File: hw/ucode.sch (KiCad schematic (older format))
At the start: 14 parts, among them U501 74HC393, U502 74HCT02, U504 74HCT238, U505 74HCT238, U506 27C64, U507 27C64, U508 27C64, U509 74HCT175, U510 74HCT175, U511 74HCT175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

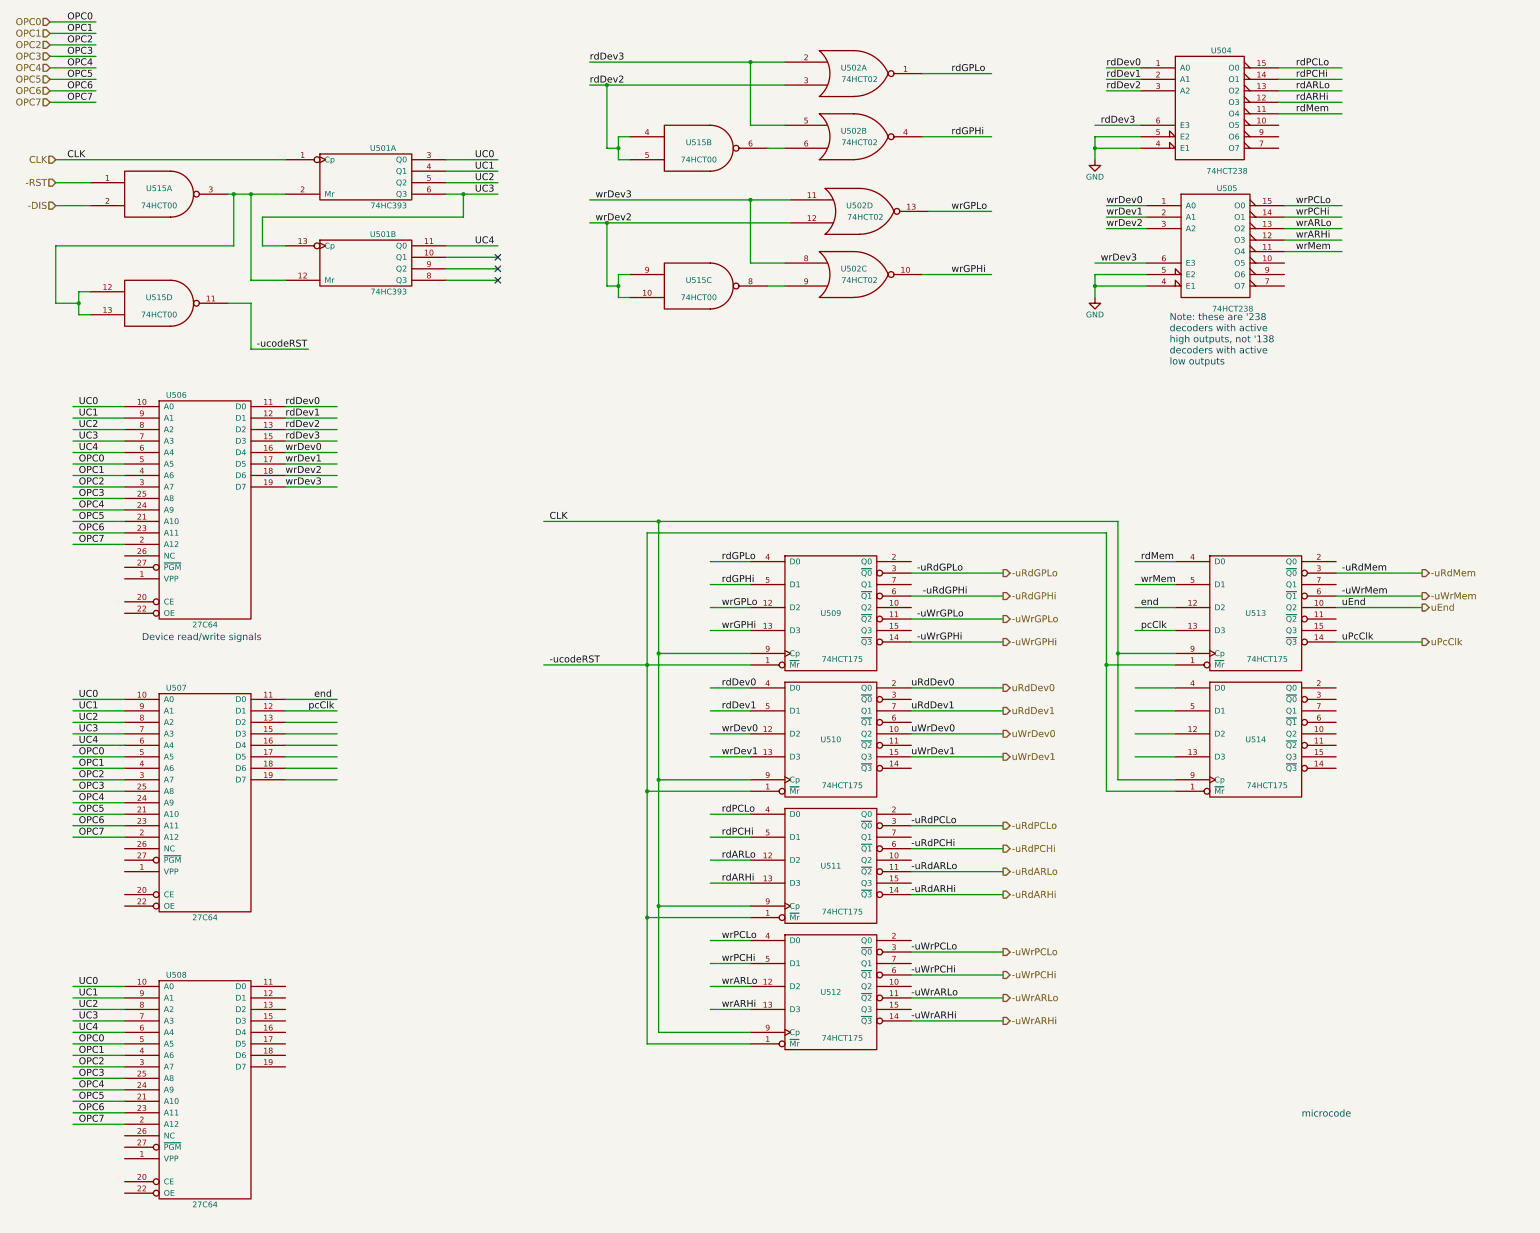
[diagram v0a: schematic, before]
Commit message: use 74HC590 as microcode program counter
The 74HC393 can only advance bit 5 using a ripple
carry from the lower 4 bit counter, which I am
concerned would be too slow (especially given the
slowness of the microcode EPROMS, which
must generate a value output within a half
of one clock cycle).  The 74HC590 is a
proper 8 bit counter, which I assume has fast
carry logic internally.
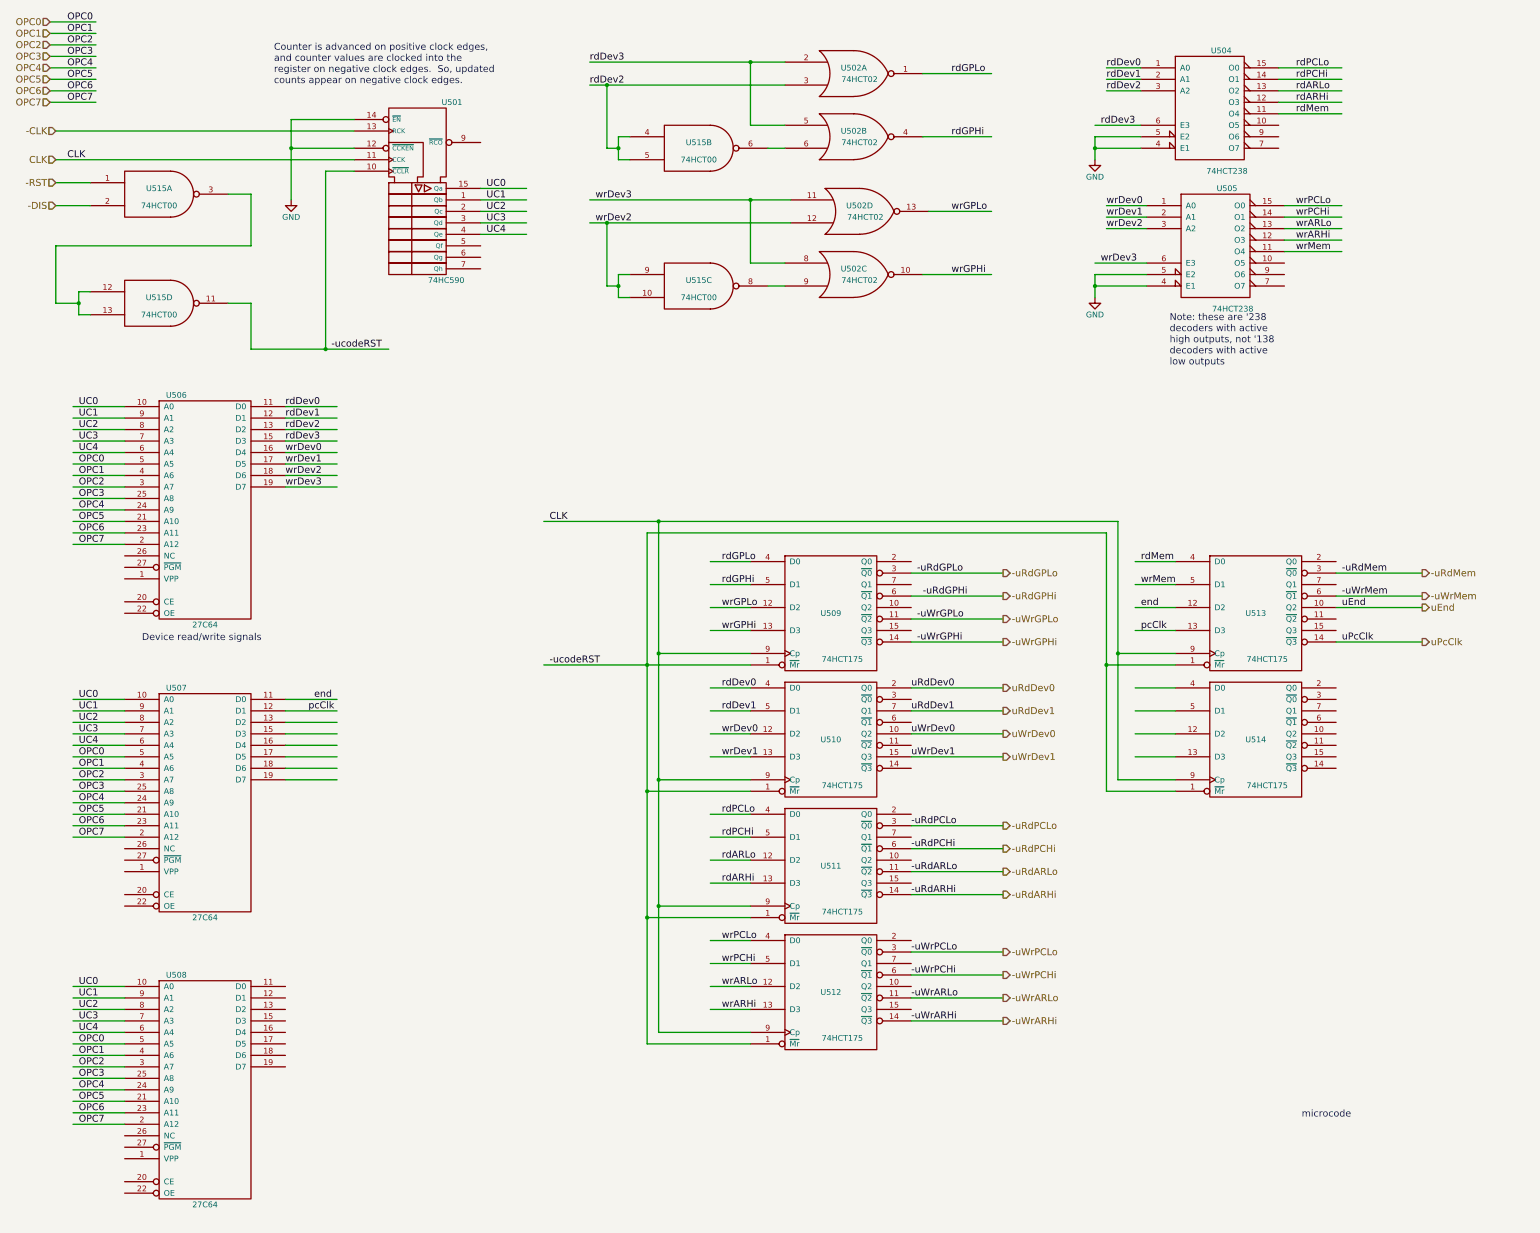
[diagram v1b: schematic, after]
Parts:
- removed U501: 74HC393, symbol 74LS393
- added U501: 74HC590, symbol 74LS590
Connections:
- net labels added: -CLK
- wire segments 223 -> 198
- no-connect marks 3 -> 0
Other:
- note added: "Counter is advanced on positive clock edges,\nand counter values are clocked into the\nregister on negative clock edges. So, updated\ncounts appear on negative clock edges."
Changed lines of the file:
@@
 LIBS:valves
 LIBS:switches
+LIBS:ttl_ieee
 LIBS:cpu2-cache
 EELAYER 25 0
@@
 	1    0    0    -1
 $EndComp
-$Comp
-L 74LS393 U501
-U 1 1 592C73B2
-P 3800 2000
-F 0 "U501" H 3950 2250 50  0000 C CNN
-F 1 "74HC393" H 4000 1750 50  0000 C CNN
-F 2 "" H 3800 2000 50  0000 C CNN
-F 3 "" H 3800 2000 50  0000 C CNN
-	1    3800 2000
-	1    0    0    -1
-$EndComp
-$Comp
-L 74LS393 U501
-U 2 1 592C73E9
-P 3800 2750
-F 0 "U501" H 3950 3000 50  0000 C CNN
-F 1 "74HC393" H 4000 2500 50  0000 C CNN
-F 2 "" H 3800 2750 50  0000 C CNN
-F 3 "" H 3800 2750 50  0000 C CNN
-	2    3800 2750
-	1    0    0    -1
-$EndComp
 Text Label 1200 650  0    60   ~ 0
 OPC0
@@
 Text Label 1200 1350 0    60   ~ 0
 OPC7
-Text Label 4750 1850 0    60   ~ 0
-UC0
-Text Label 4750 1950 0    60   ~ 0
-UC1
-Text Label 4750 2050 0    60   ~ 0
-UC2
-Text Label 4750 2150 0    60   ~ 0
-UC3
-Text Label 4750 2600 0    60   ~ 0
-UC4
 Text Label 1300 4000 0    60   ~ 0
 UC0
@@
 Text Label 1300 10250 0    60   ~ 0
 OPC7
-NoConn ~ 4950 2700
-NoConn ~ 4950 2800
-NoConn ~ 4950 2900
 Text Notes 11950 10200 0    60   ~ 0
 microcode
@@
 	1050 1350 1450 1350
 Wire Wire Line
-	4500 2150 4650 2150
-Wire Wire Line
-	4650 2150 4950 2150
-Wire Wire Line
-	4650 2150 4650 2350
-Wire Wire Line
-	4650 2350 2900 2350
-Wire Wire Line
-	2900 2350 2900 2600
-Wire Wire Line
-	2900 2600 3100 2600
-Wire Wire Line
-	4500 1850 4950 1850
-Wire Wire Line
-	4500 1950 4950 1950
-Wire Wire Line
-	4500 2050 4950 2050
-Connection ~ 4650 2150
-Wire Wire Line
-	4500 2600 4950 2600
-Wire Wire Line
 	1700 4000 1250 4000
 Wire Wire Line
@@
 	1700 10250 1250 10250
 Wire Wire Line
-	4500 2700 4950 2700
-Wire Wire Line
-	4500 2800 4950 2800
-Wire Wire Line
-	4500 2900 4950 2900
-Wire Wire Line
-	2600 2150 2650 2150
-Wire Wire Line
-	2650 2150 2800 2150
-Wire Wire Line
-	2800 2150 3100 2150
-Wire Wire Line
-	3100 2900 2800 2900
-Wire Wire Line
-	2800 2900 2800 2150
-Connection ~ 2800 2150
-Wire Wire Line
-	1100 1850 3100 1850
+	1100 1850 3700 1850
 Wire Wire Line
 	3100 4000 3550 4000
@@
 	10150 1750 10550 1750
 Wire Wire Line
-	10150 1650 10150 1750
-Wire Wire Line
-	10150 1750 10150 1850
+	10150 1650 10150 1850
 Wire Wire Line
 	10550 1050 10250 1050
@@
 	10600 2950 10150 2950
 Wire Wire Line
-	10150 2850 10150 2950
-Wire Wire Line
-	10150 2950 10150 3050
+	10150 2850 10150 3050
 Wire Wire Line
 	11800 2250 12300 2250
@@
 	11800 2650 12300 2650
 Wire Wire Line
-	5750 1000 7150 1000
-Wire Wire Line
-	7150 1000 7450 1000
-Wire Wire Line
-	5750 1200 5900 1200
-Wire Wire Line
-	5900 1200 7450 1200
-Wire Wire Line
-	5750 2200 7150 2200
-Wire Wire Line
-	7150 2200 7500 2200
-Wire Wire Line
-	5750 2400 5900 2400
-Wire Wire Line
-	5900 2400 7500 2400
+	5750 1000 7450 1000
+Wire Wire Line
+	5750 1200 7450 1200
+Wire Wire Line
+	5750 2200 7500 2200
+Wire Wire Line
+	5750 2400 7500 2400
 Wire Wire Line
 	8650 1100 9250 1100
@@
 	6100 2850 6000 2850
 Wire Wire Line
-	6000 2850 6000 2950
-Wire Wire Line
-	6000 2950 6000 3050
+	6000 2850 6000 3050
 Wire Wire Line
 	6000 2950 5900 2950
@@
 	1400 3000 1300 3000
 Wire Wire Line
-	1300 3000 1300 3100
-Wire Wire Line
-	1300 3100 1300 3200
+	1300 3000 1300 3200
 Wire Wire Line
 	1300 3100 1100 3100
@@
 	1100 3100 1100 2600
 Wire Wire Line
-	1100 2600 2650 2600
-Wire Wire Line
-	2650 2600 2650 2150
-Connection ~ 2650 2150
+	1100 2600 2800 2600
+Wire Wire Line
+	2800 2600 2800 2150
 Wire Wire Line
 	1300 3200 1400 3200
@@
 	2800 3100 2800 3500
 Wire Wire Line
-	2800 3500 3300 3500
-Text Label 2850 3500 0    60   ~ 0
+	2800 3500 4000 3500
+Text Label 3500 3500 0    60   ~ 0
 -ucodeRST
 Wire Wire Line
-	5350 6250 6250 6250
-Wire Wire Line
-	6250 6250 7150 6250
+	5350 6250 7150 6250
 Text Label 5400 6250 0    60   ~ 0
 -ucodeRST
@@
 	6250 7350 7150 7350
 Wire Wire Line
-	6250 5100 6250 6250
-Wire Wire Line
-	6250 6250 6250 7350
-Wire Wire Line
-	6250 7350 6250 8450
-Wire Wire Line
-	6250 8450 6250 9550
+	6250 5100 6250 9550
 Connection ~ 6250 6250
 Wire Wire Line
@@
 	10850 6250 10250 6250
 Wire Wire Line
-	10250 5100 10250 6250
-Wire Wire Line
-	10250 6250 10250 7350
+	10250 5100 10250 7350
 Wire Wire Line
 	10250 5100 6250 5100
@@
 	7150 6150 6350 6150
 Wire Wire Line
-	6350 5000 6350 6150
-Wire Wire Line
-	6350 6150 6350 7250
-Wire Wire Line
-	6350 7250 6350 8350
-Wire Wire Line
-	6350 8350 6350 9450
-Wire Wire Line
-	5350 5000 6350 5000
-Wire Wire Line
-	6350 5000 10350 5000
+	6350 5000 6350 9450
+Wire Wire Line
+	5350 5000 10350 5000
 Text Label 5400 5000 0    60   ~ 0
 CLK
@@
 	10850 6150 10350 6150
 Wire Wire Line
-	10350 5000 10350 6150
-Wire Wire Line
-	10350 6150 10350 7250
+	10350 5000 10350 7250
 Connection ~ 6350 5000
 Wire Wire Line
@@
 	6000 1750 5900 1750
 Wire Wire Line
-	6000 1650 6000 1750
-Wire Wire Line
-	6000 1750 6000 1850
+	6000 1650 6000 1850
 Wire Wire Line
 	6100 1650 6000 1650
@@
 	1    0    0    -1
 $EndComp
+$Comp
+L 74LS590 U501
+U 1 1 594FEAE3
+P 4250 2150
+F 0 "U501" H 4550 2950 50  0000 C CNN
+F 1 "74HC590" H 4500 1400 50  0000 C CNN
+F 2 "" H 4250 2150 60  0000 C CNN
+F 3 "" H 4250 2150 60  0000 C CNN
+	1    4250 2150
+	1    0    0    -1
+$EndComp
+Text HLabel 1100 1600 0    60   Input ~ 0
+-CLK
+Wire Wire Line
+	3700 1600 1100 1600
+Wire Wire Line
+	3700 1950 3450 1950
+Wire Wire Line
+	3450 1950 3450 3500
+Connection ~ 3450 3500
+Wire Wire Line
+	2800 2150 2600 2150
+Wire Wire Line
+	3700 1750 3150 1750
+Wire Wire Line
+	3150 1500 3150 2200
+Wire Wire Line
+	3700 1500 3150 1500
+Connection ~ 3150 1750
+Wire Wire Line
+	4800 2100 5200 2100
+Wire Wire Line
+	4800 2200 5200 2200
+Wire Wire Line
+	4800 2300 5200 2300
+Wire Wire Line
+	4800 2400 5200 2400
+Wire Wire Line
+	4800 2500 5200 2500
+Text Label 4850 2100 0    60   ~ 0
+UC0
+Text Label 4850 2200 0    60   ~ 0
+UC1
+Text Label 4850 2300 0    60   ~ 0
+UC2
+Text Label 4850 2400 0    60   ~ 0
+UC3
+Text Label 4850 2500 0    60   ~ 0
+UC4
+$Comp
+L GND #PWR?
+U 1 1 59500711
+P 3150 2200
+F 0 "#PWR?" H 3150 1950 50  0001 C CNN
+F 1 "GND" H 3150 2050 50  0000 C CNN
+F 2 "" H 3150 2200 50  0001 C CNN
+F 3 "" H 3150 2200 50  0001 C CNN
+	1    3150 2200
+	1    0    0    -1
+$EndComp
+Text Notes 3000 1200 0    60   ~ 0
+Counter is advanced on positive clock edges,\nand counter values are clocked into the\nregister on negative clock edges.  So, updated\ncounts appear on negative clock edges.
 $EndSCHEMATC

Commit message: redoing device read logic
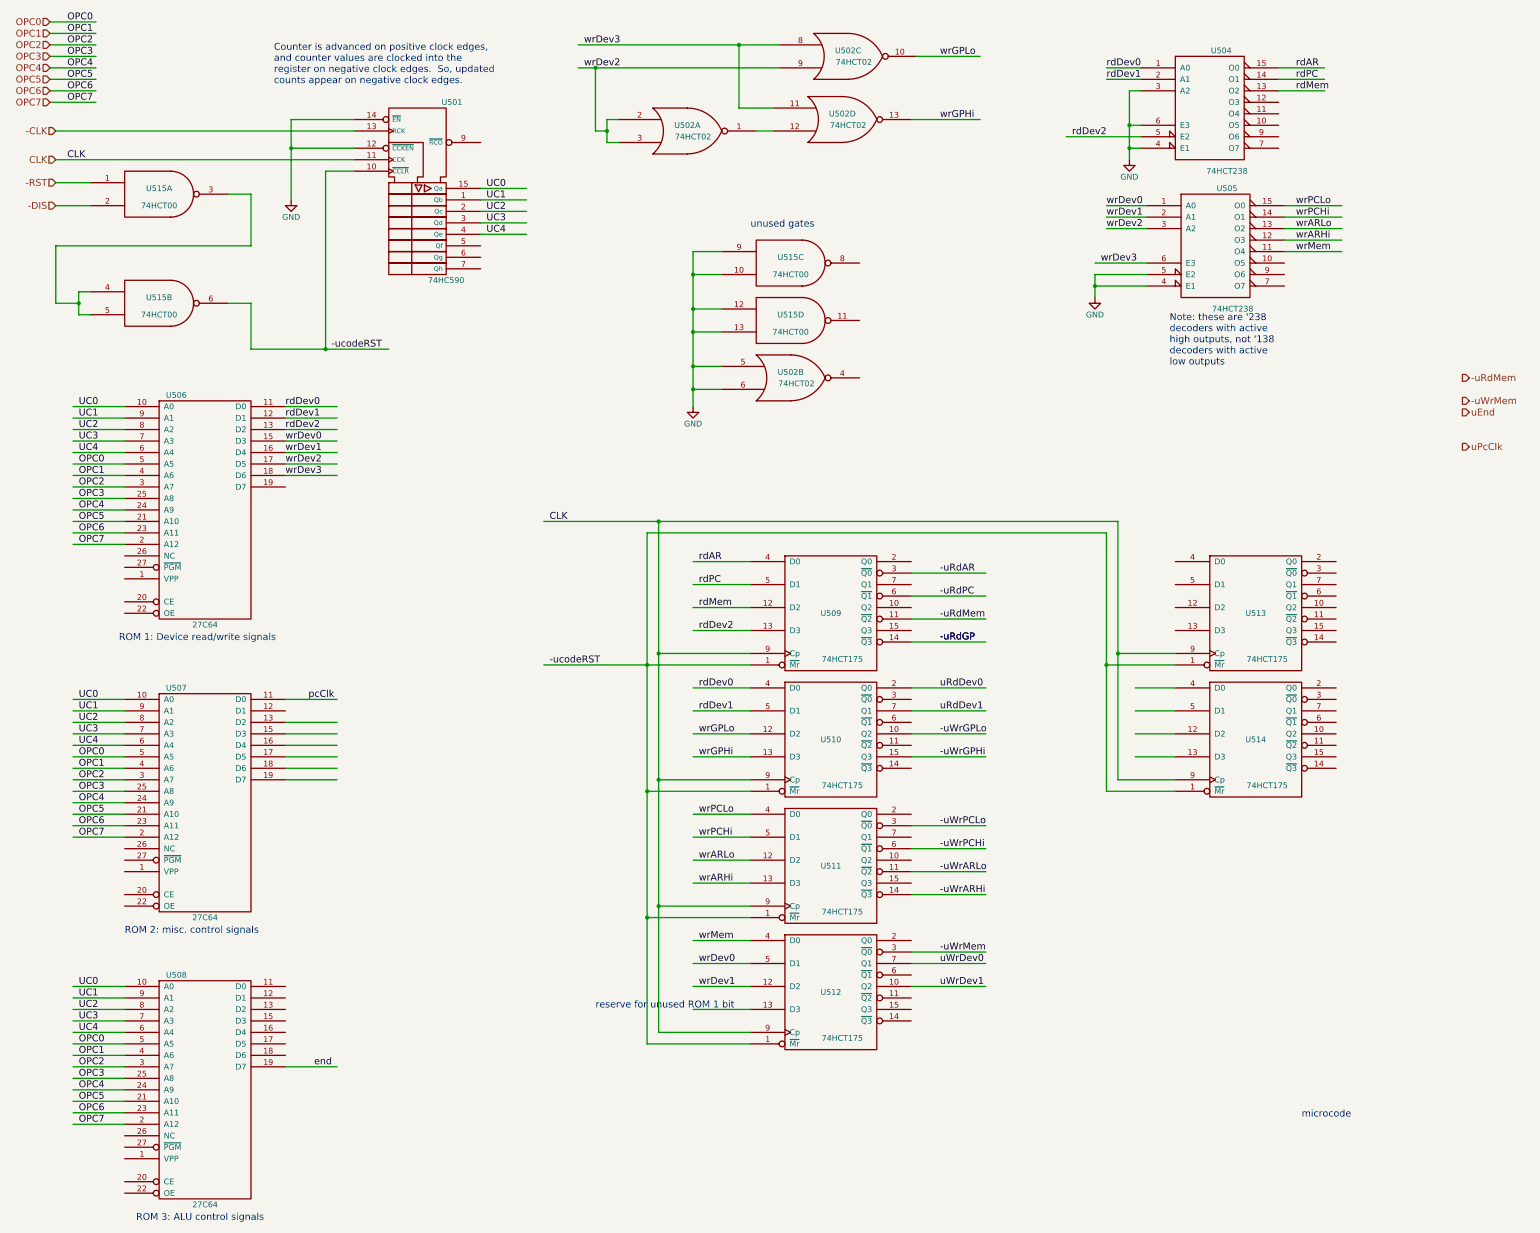
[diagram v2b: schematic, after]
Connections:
- net labels added: -uRdAR, -uRdGP, -uRdPC, rdAR, rdPC
- net labels removed: -uRdARHi, -uRdARLo, -uRdGPHi, -uRdGPLo, -uRdPCHi, -uRdPCLo, rdARHi, rdARLo, rdDev3, rdGPHi, rdGPLo, rdPCHi, rdPCLo
- wire segments 198 -> 205
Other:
- note added: "ROM 1: Device read/write signals"
- note added: "ROM 2: misc. control signals"
- note added: "ROM 3: ALU control signals"
- note added: "reserve for unused ROM 1 bit"
- note added: "unused gates"
- note removed: "Device read/write signals"
- moved on the sheet: U502A, U502B, U502C, U502D, U515B, U515C, U515D

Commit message: more redesign of microcode
Reading and writing devices and ALU control are
mostly in place.

Eliminated the dedicated signals to assert device pairs
to the left/right ALU input busses.  These aren't needed
any more because all reading from devices is done using
pairs (with the ALU to select which one is copied to the
ALU data bus.)
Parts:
- added U515, U516: 74HCT175, symbol 74LS175
- renumbered U515 to U520
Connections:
- net labels added: -uAluCarryIn, -uAluOut, -uDriveAddr, aluCarryIn, aluMode, aluOp0, aluOp1, aluOp2, aluOp3, aluOut, driveAddr, uAluMode, uAluOp0, uAluOp1, uAluOp2, uAluOp3
- wire segments 205 -> 215
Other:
- moved on the sheet: U513, U514
